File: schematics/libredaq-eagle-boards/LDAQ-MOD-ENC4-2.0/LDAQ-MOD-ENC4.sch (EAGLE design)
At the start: 25 parts, among them CON1 BOARD, IC1 5M240ZT100A5N, IC2 NCP164CSN180T1G, IC3 NXB0104PWJ, IC4 NXB0104PWJ, J1 SCREWTERMINAL-3.5MM-5, J2 SCREWTERMINAL-3.5MM-5, J3 70246-1004

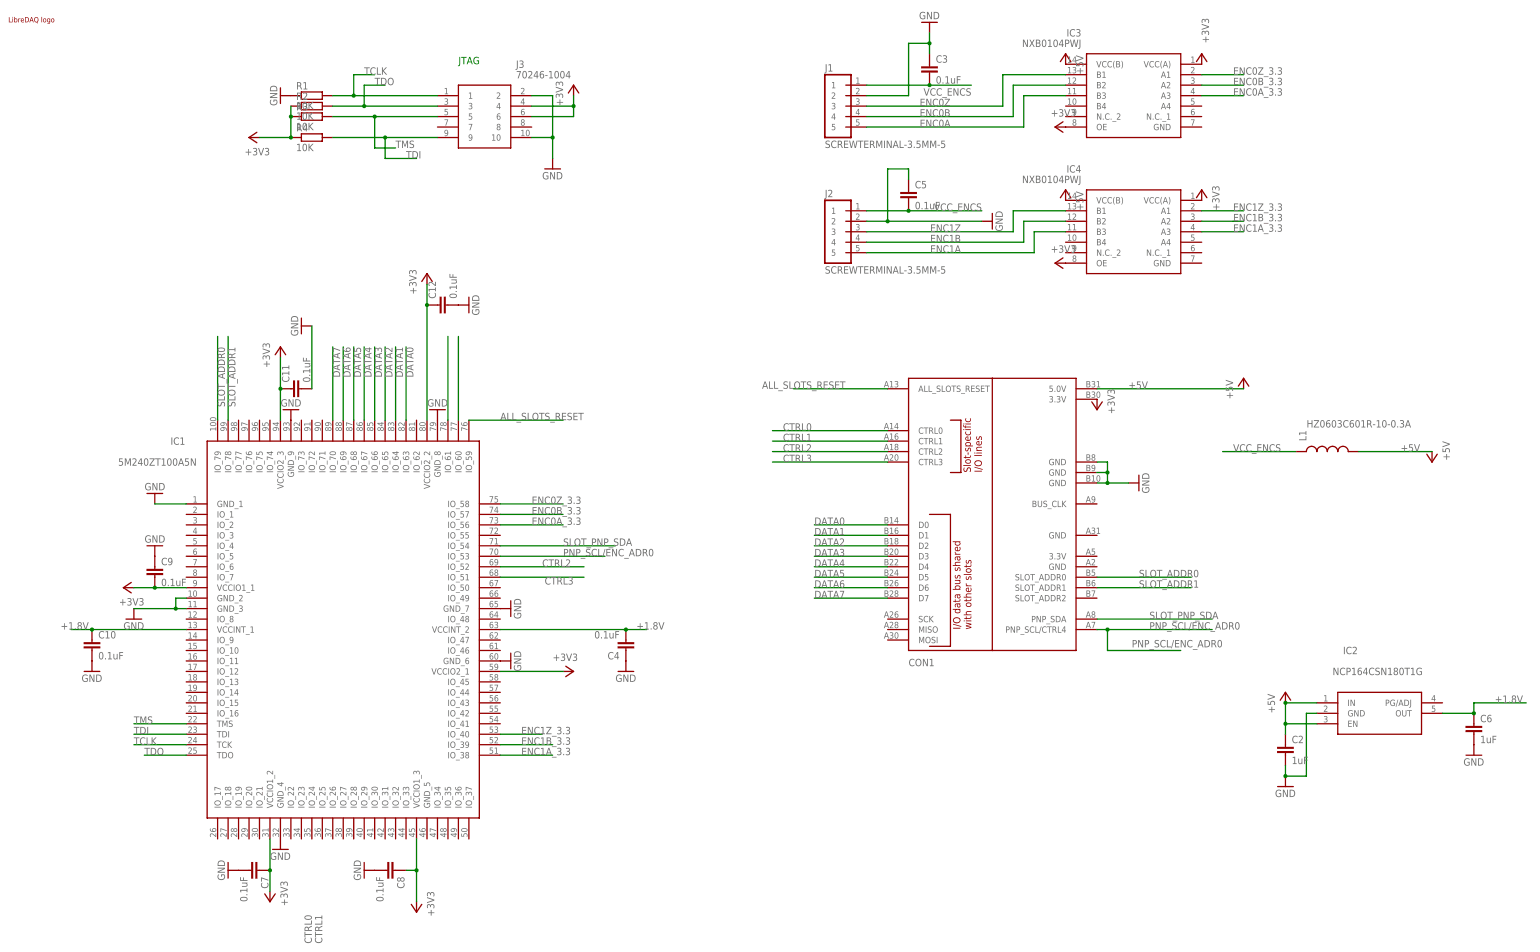
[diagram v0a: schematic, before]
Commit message: Start upgrade to another FPGA
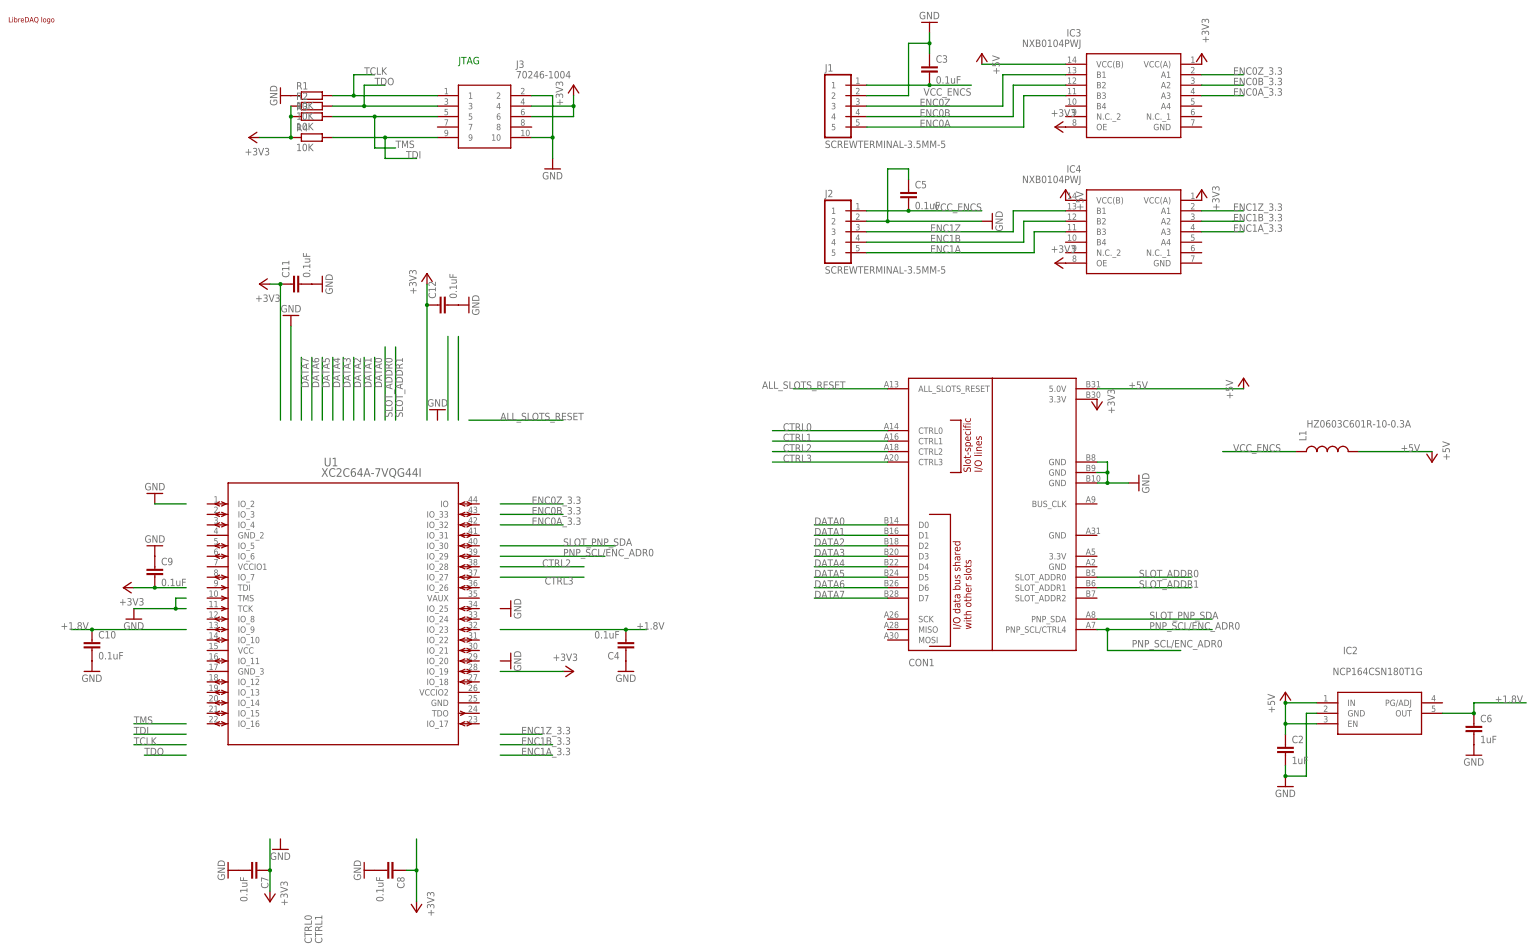
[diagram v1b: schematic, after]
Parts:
- removed IC1: 5M240ZT100A5N, 5M240ZT100A5N:5M240ZT100A5N
- added U1: XC2C64A-7VQG44I, XC2C64A-7VQG44I:XC2C64A-7VQG44I
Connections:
- net +1.8V: no longer IC1.VCCINT_1, IC1.VCCINT_2
- net +3V3: no longer IC1.VCCIO1_1, IC1.VCCIO1_2, IC1.VCCIO1_3, IC1.VCCIO2_1, IC1.VCCIO2_2, IC1.VCCIO2_3
- net ALL_SLOTS_RESET: no longer IC1.IO_59
- net CTRL0: no longer IC1.IO_60
- net CTRL1: no longer IC1.IO_61
- net CTRL2: no longer IC1.IO_52
- net CTRL3: no longer IC1.IO_51
- net DATA0: no longer IC1.IO_63
- net DATA1: no longer IC1.IO_64
- net DATA2: no longer IC1.IO_65
- net DATA3: no longer IC1.IO_66
- net DATA4: no longer IC1.IO_67
- net DATA5: no longer IC1.IO_68
- net DATA6: no longer IC1.IO_69
- net DATA7: no longer IC1.IO_70
- net ENC0A_3.3: no longer IC1.IO_56
- net ENC0B_3.3: no longer IC1.IO_57
- net ENC0Z_3.3: no longer IC1.IO_58
- net ENC1A_3.3: no longer IC1.IO_38
- net ENC1B_3.3: no longer IC1.IO_39
- net ENC1Z_3.3: no longer IC1.IO_40
- net GND: no longer IC1.GND_1, IC1.GND_2, IC1.GND_3, IC1.GND_4, IC1.GND_6, IC1.GND_7, IC1.GND_8, IC1.GND_9
- net PNP_SCL/ENC_ADR0: no longer IC1.IO_53
- net SLOT_ADDR0: no longer IC1.IO_79
- net SLOT_ADDR1: no longer IC1.IO_78
- net SLOT_PNP_SDA: no longer IC1.IO_54
- net TCLK: no longer IC1.TCK
- net TDI: no longer IC1.TDI
- net TDO: no longer IC1.TDO
- net TMS: no longer IC1.TMS
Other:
- moved on the sheet: C11
